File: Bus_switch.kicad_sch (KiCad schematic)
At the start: 8 parts, among them J3 Conn_01x04_Pin, U1 SN74CB3Q3245PWR

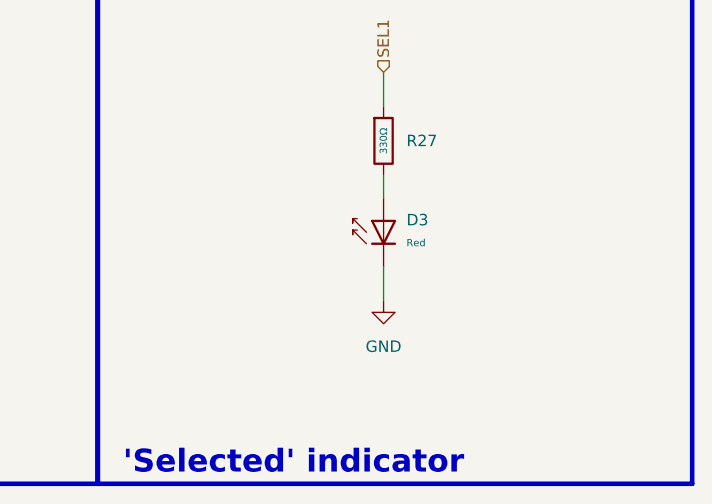
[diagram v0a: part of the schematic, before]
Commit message: fixed selected led polarity
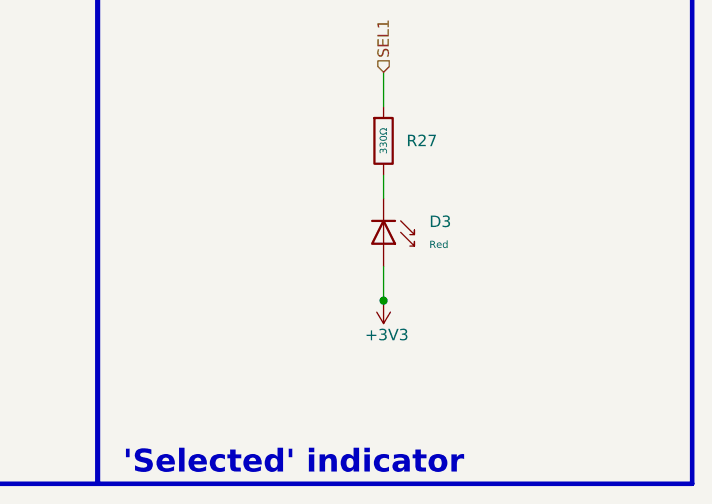
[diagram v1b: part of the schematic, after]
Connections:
- net +3V3: now also D3.2
- net GND: no longer D3.1
- net at R27.2: now also D3.1; no longer D3.2
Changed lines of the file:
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@@
 		(color 0 0 0 0)
 	)
+	(junction
+		(at 248.92 134.5952)
+		(diameter 0)
+		(color 0 0 0 0)
+	)
 	(no_connect
 		(at 60.96 88.9)
@@
 	(wire
 		(pts
-			(xy 248.92 130.81) (xy 248.92 134.62)
+			(xy 248.92 130.81) (xy 248.92 134.5952)
 		)
 		(stroke
@@
 		)
 	)
+	(wire
+		(pts
+			(xy 248.92 134.5952) (xy 248.92 134.62)
+		)
+		(stroke
+			(width 0)
+			(type default)
+		)
+	)
 	(bus
 		(pts
@@
 	)
 	(symbol
-		(lib_id "power:GND")
-		(at 248.92 134.62 0)
+		(lib_id "PCM_JLCPCB-Diodes:LED,0603,Red")
+		(at 248.92 127 180)
 		(unit 1)
 		(body_style 1)
@@
 		(dnp no)
 		(fields_autoplaced yes)
-		(property "Reference" "#PWR0107"
-			(at 248.92 140.97 0)
+		(property "Reference" "D3"
+			(at 254 125.8251 0)
+			(show_name no)
+			(do_not_autoplace no)
+			(effects
+				(font
+					(size 1.27 1.27)
+				)
+				(justify right)
+			)
+		)
+		(property "Value" "Red"
+			(at 254 128.3652 0)
+			(show_name no)
+			(do_not_autoplace no)
+			(effects
+				(font
+					(size 0.8 0.8)
+				)
+				(justify right)
+			)
+		)
+		(property "Footprint" "PCM_JLCPCB:D_0603"
+			(at 250.698 127 90)
 			(hide yes)
 			(show_name no)
@@
 			)
 		)
-		(property "Value" "GND"
-			(at 248.92 139.7 0)
+		(property "Datasheet" "https://www.lcsc.com/datasheet/lcsc_datasheet_1810231112_Hubei-KENTO-Elec-KT-0603R_C2286.pdf"
+			(at 248.92 127 0)
+			(hide yes)
 			(show_name no)
 			(do_not_autoplace no)
@@
 			)
 		)
-		(property "Footprint" ""
-			(at 248.92 134.62 0)
+		(property "Description" "-40°C~+85°C Red 0603 LED Indication - Discrete ROHS"
+			(at 248.92 127 0)
 			(hide yes)
 			(show_name no)
@@
 			)
 		)
-		(property "Datasheet" ""
-			(at 248.92 134.62 0)
+		(property "LCSC" "C2286"
+			(at 248.92 127 0)
 			(hide yes)
 			(show_name no)
@@
 			)
 		)
-		(property "Description" "Power symbol creates a global label with name \"GND\" , ground"
-			(at 248.92 134.62 0)
+		(property "Stock" "5373336"
+			(at 248.92 127 0)
+			(hide yes)
+			(show_name no)
+			(do_not_autoplace no)
+			(effects
+				(font
+					(size 1.27 1.27)
+				)
+			)
+		)
+		(property "Price" "0.009USD"
+			(at 248.92 127 0)
+			(hide yes)
+			(show_name no)
+			(do_not_autoplace no)
+			(effects
+				(font
+					(size 1.27 1.27)
+				)
+			)
+		)
+		(property "Process" "SMT"
+			(at 248.92 127 0)
+			(hide yes)
+			(show_name no)
+			(do_not_autoplace no)
+			(effects
+				(font
+					(size 1.27 1.27)
+				)
+			)
+		)
+		(property "Minimum Qty" "20"
+			(at 248.92 127 0)
+			(hide yes)
+			(show_name no)
+			(do_not_autoplace no)
+			(effects
+				(font
+					(size 1.27 1.27)
+				)
+			)
+		)
+		(property "Attrition Qty" "10"
+			(at 248.92 127 0)
+			(hide yes)
+			(show_name no)
+			(do_not_autoplace no)
+			(effects
+				(font
+					(size 1.27 1.27)
+				)
+			)
+		)
+		(property "Class" "Basic Component"
+			(at 248.92 127 0)
+			(hide yes)
+			(show_name no)
+			(do_not_autoplace no)
+			(effects
+				(font
+					(size 1.27 1.27)
+				)
+			)
+		)
+		(property "Category" "Optocouplers & LEDs & Infrared,Light Emitting Diodes (LED)"
+			(at 248.92 127 0)
+			(hide yes)
+			(show_name no)
+			(do_not_autoplace no)
+			(effects
+				(font
+					(size 1.27 1.27)
+				)
+			)
+		)
+		(property "Manufacturer" "Hubei KENTO Elec"
+			(at 248.92 127 0)
+			(hide yes)
+			(show_name no)
+			(do_not_autoplace no)
+			(effects
+				(font
+					(size 1.27 1.27)
+				)
+			)
+		)
+		(property "Part" "KT-0603R"
+			(at 248.92 127 0)
 			(hide yes)
 			(show_name no)
@@
 			)
 		)
+		(pin "2"
+		)
 		(pin "1"
 		)
@@
 			(project "MMS3_hat_HC-SR04-HX711"
 				(path "/6596548a-44e0-46d8-8624-fd71cf4a3e17/ec6d73af-72b0-4068-85fb-cca3c5143749"
-					(reference "#PWR0107")
+					(reference "D3")
 					(unit 1)
 				)
@@
 	)
 	(symbol
-		(lib_id "PCM_JLCPCB-Diodes:LED,0603,Red")
-		(at 248.92 127 0)
+		(lib_id "power:+5V")
+		(at 248.92 134.5952 180)
 		(unit 1)
 		(body_style 1)
@@
 		(in_pos_files yes)
 		(dnp no)
-		(fields_autoplaced yes)
-		(property "Reference" "D3"
-			(at 251.46 125.6346 0)
-			(show_name no)
-			(do_not_autoplace no)
-			(effects
-				(font
-					(size 1.27 1.27)
-				)
-				(justify left)
-			)
-		)
-		(property "Value" "Red"
-			(at 251.46 128.1747 0)
-			(show_name no)
-			(do_not_autoplace no)
-			(effects
-				(font
-					(size 0.8 0.8)
-				)
-				(justify left)
-			)
-		)
-		(property "Footprint" "PCM_JLCPCB:D_0603"
-			(at 247.142 127 90)
+		(property "Reference" "#PWR0114"
+			(at 248.92 130.7852 0)
 			(hide yes)
 			(show_name no)
@@
 			)
 		)
-		(property "Datasheet" "https://www.lcsc.com/datasheet/lcsc_datasheet_1810231112_Hubei-KENTO-Elec-KT-0603R_C2286.pdf"
-			(at 248.92 127 0)
-			(hide yes)
-			(show_name no)
-			(do_not_autoplace no)
-			(effects
-				(font
-					(size 1.27 1.27)
-				)
-			)
-		)
-		(property "Description" "-40°C~+85°C Red 0603 LED Indication - Discrete ROHS"
-			(at 248.92 127 0)
-			(hide yes)
-			(show_name no)
-			(do_not_autoplace no)
-			(effects
-				(font
-					(size 1.27 1.27)
-				)
-			)
-		)
-		(property "LCSC" "C2286"
-			(at 248.92 127 0)
-			(hide yes)
-			(show_name no)
-			(do_not_autoplace no)
-			(effects
-				(font
-					(size 1.27 1.27)
-				)
-			)
-		)
-		(property "Stock" "5373336"
-			(at 248.92 127 0)
-			(hide yes)
-			(show_name no)
-			(do_not_autoplace no)
-			(effects
-				(font
-					(size 1.27 1.27)
-				)
-			)
-		)
-		(property "Price" "0.009USD"
-			(at 248.92 127 0)
-			(hide yes)
-			(show_name no)
-			(do_not_autoplace no)
-			(effects
-				(font
-					(size 1.27 1.27)
-				)
-			)
-		)
-		(property "Process" "SMT"
-			(at 248.92 127 0)
-			(hide yes)
-			(show_name no)
-			(do_not_autoplace no)
-			(effects
-				(font
-					(size 1.27 1.27)
-				)
-			)
-		)
-		(property "Minimum Qty" "20"
-			(at 248.92 127 0)
-			(hide yes)
-			(show_name no)
-			(do_not_autoplace no)
-			(effects
-				(font
-					(size 1.27 1.27)
-				)
-			)
-		)
-		(property "Attrition Qty" "10"
-			(at 248.92 127 0)
-			(hide yes)
-			(show_name no)
-			(do_not_autoplace no)
-			(effects
-				(font
-					(size 1.27 1.27)
-				)
-			)
-		)
-		(property "Class" "Basic Component"
-			(at 248.92 127 0)
-			(hide yes)
+		(property "Value" "+3V3"
+			(at 251.714 138.4052 0)
 			(show_name no)
 			(do_not_autoplace no)
@@
 					(size 1.27 1.27)
 				)
+				(justify left)
 			)
 		)
-		(property "Category" "Optocouplers & LEDs & Infrared,Light Emitting Diodes (LED)"
-			(at 248.92 127 0)
+		(property "Footprint" ""
+			(at 248.92 134.5952 0)
 			(hide yes)
 			(show_name no)
@@
 			)
 		)
-		(property "Manufacturer" "Hubei KENTO Elec"
-			(at 248.92 127 0)
+		(property "Datasheet" ""
+			(at 248.92 134.5952 0)
 			(hide yes)
 			(show_name no)
@@
 			)
 		)
-		(property "Part" "KT-0603R"
-			(at 248.92 127 0)
+		(property "Description" "Power symbol creates a global label with name \"+5V\""
+			(at 248.92 134.5952 0)
 			(hide yes)
 			(show_name no)
@@
 			)
 		)
-		(pin "2"
-		)
 		(pin "1"
 		)
@@
 			(project "MMS3_hat_HC-SR04-HX711"
 				(path "/6596548a-44e0-46d8-8624-fd71cf4a3e17/ec6d73af-72b0-4068-85fb-cca3c5143749"
-					(reference "D3")
+					(reference "#PWR0114")
 					(unit 1)
 				)
